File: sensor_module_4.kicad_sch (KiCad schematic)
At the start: 34 parts, among them J1 pH_IN, J17 Atlas Surveyor, J18 EZO Carrier Board, J3 ORP_In, J4 Turbidity TSW-10, U3 ESDA5V3SC5, U4 OPA2397DGKR, U5 OPA2397DGKR

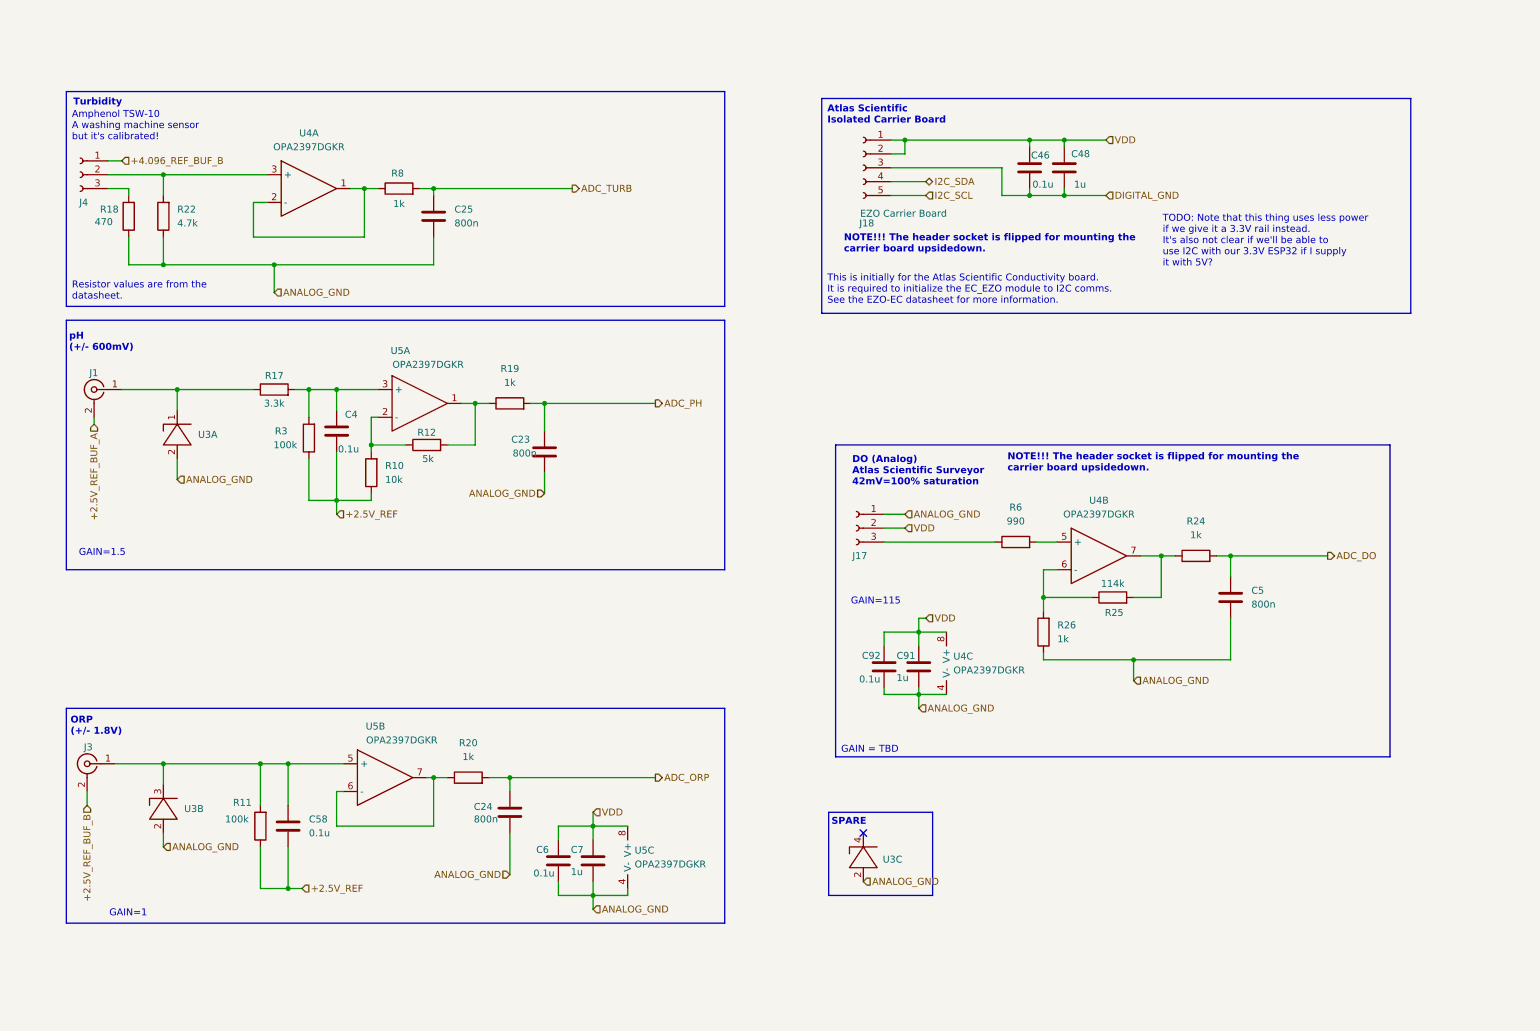
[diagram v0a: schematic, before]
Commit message: Prototype v0.3.1 WIP Just a maintenance checkin. Many changes - Removed the Base Sensor schematic and put all sensors into SensorPrototype - Added a constant current LED driver for camera illumination - Added a 12V buck converter to the input in support of external power - Added a low-side current sense to the input - Added an LDO regulator to cleanup Buck output and to provide battery regulation - Added support for an internal battery + switchover / charge circuit. - Swapped headers for proper board connectors - Added an RS485 transceiver for external + modem communication - Added an additional temperature circuit in support of NTC probes - Incorporated the AS Dissolved Oxygen sensor into the main board - Added DC return path resistors to non-inverting amps - Fixed mixed power domain bug - Moved AS isolated carrier board to 3.3V rail and routed the shutdown pin to en/sh - Moved the DHT20 to the 3.3V rail - In the process of re-routing ADC channels.
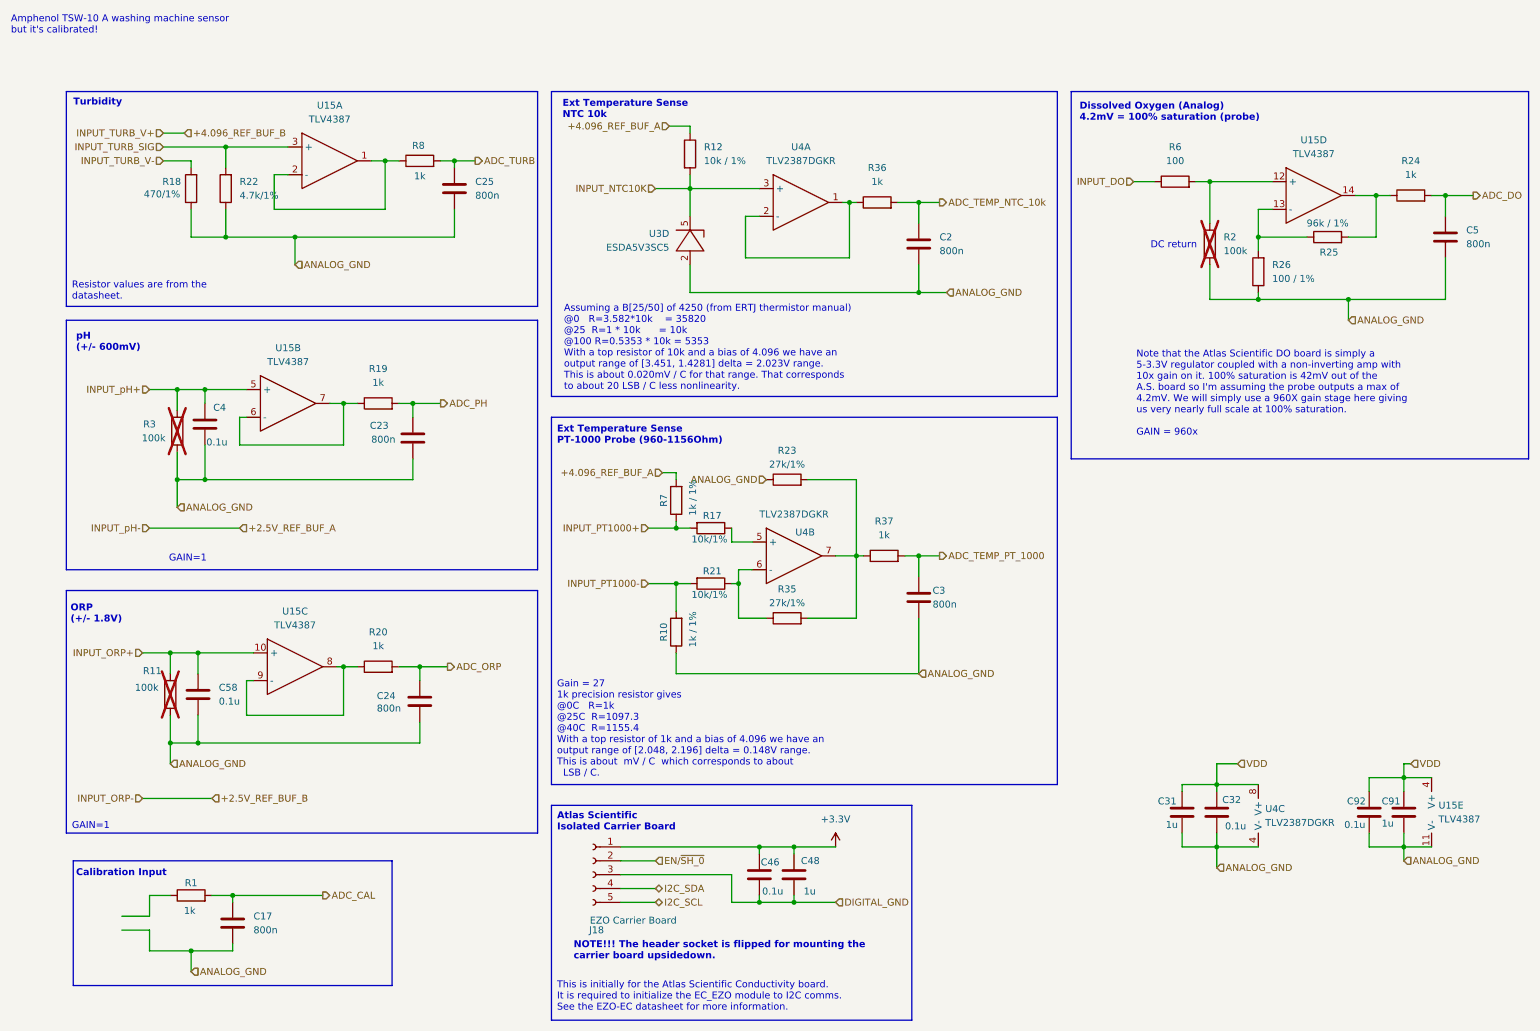
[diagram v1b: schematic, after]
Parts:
- removed C6: 0.1u, Capacitor_SMD:C_1210_3225Metric_Pad1.33x2.70mm_HandSolder, symbol Device:C
- removed C7: 1u, Capacitor_SMD:C_1210_3225Metric_Pad1.33x2.70mm_HandSolder, symbol Device:C
- removed J1: pH_IN, Connector_PinHeader_2.54mm:PinHeader_1x02_P2.54mm_Vertical_SMD_Pin1Left, symbol Connector:Conn_Coaxial
- removed J17: Atlas Surveyor, Connector_PinSocket_2.54mm:PinSocket_1x03_P2.54mm_Vertical, symbol Connector:Conn_01x03_Socket
- removed J3: ORP_In, Connector_PinHeader_2.54mm:PinHeader_1x02_P2.54mm_Vertical_SMD_Pin1Left, symbol Connector:Conn_Coaxial
- removed J4: Turbidity TSW-10, Connector_PinHeader_2.54mm:PinHeader_1x03_P2.54mm_Vertical_SMD_Pin1Left, symbol Connector:Conn_01x03_Socket
- removed U3: ESDA5V3SC5, Package_TO_SOT_SMD:SOT-23-5, symbol AndrewAdditions:sda5v3sc6_split
- removed U4, U5: OPA2397DGKR, Package_SO:SOIC-8_3.9x4.9mm_P1.27mm, symbol Op-Amp-Extended:OPA2397DR
- added C17, C2, C3: 800n, Capacitor_SMD:C_0805_2012Metric_Pad1.18x1.45mm_HandSolder, symbol Device:C
- added C31: 1u, Capacitor_SMD:C_0805_2012Metric_Pad1.18x1.45mm_HandSolder, symbol Device:C
- added C32: 0.1u, Capacitor_SMD:C_0805_2012Metric_Pad1.18x1.45mm_HandSolder, symbol Device:C
- added R1, R36, R37: 1k, Resistor_SMD:R_0805_2012Metric_Pad1.20x1.40mm_HandSolder, symbol Device:R
- added R2: 100k, Resistor_SMD:R_0805_2012Metric_Pad1.20x1.40mm_HandSolder, symbol Device:R
- added R21: 10k/1%, Resistor_SMD:R_0805_2012Metric_Pad1.20x1.40mm_HandSolder, symbol Device:R
- added R23, R35: 27k/1%, Resistor_SMD:R_0805_2012Metric_Pad1.20x1.40mm_HandSolder, symbol Device:R
- added R7: 1k / 1%, Resistor_SMD:R_0805_2012Metric_Pad1.20x1.40mm_HandSolder, symbol Device:R
- added U15: TLV4387, Package_SO:TSSOP-14_4.4x5mm_P0.65mm, symbol Op-Amp-Extended:TLV4387PWR
- added U3: ESDA5V3SC5, Package_TO_SOT_SMD:SOT-23-5, symbol AndrewAdditions:sda5v3sc6_split
- added U4: TLV2387DGKR, Package_SO:VSSOP-8_3x3mm_P0.65mm, symbol Op-Amp-Extended:TLV2387DGKR
- C23, C24, C25, C4, C46, C48, C5, C58, C91, C92: footprint Capacitor_SMD:C_1210_3225Metric_Pad1.33x2.70mm_HandSolder -> Capacitor_SMD:C_0805_2012Metric_Pad1.18x1.45mm_HandSolder
- J18: footprint Connector_PinSocket_2.54mm:PinSocket_1x05_P2.54mm_Vertical -> Connector_PinSocket_2.54mm:PinSocket_1x05_P2.54mm_Vertical_SMD_Pin1Left
- R10: value 10k -> 1k / 1%; footprint Resistor_SMD:R_1210_3225Metric_Pad1.30x2.65mm_HandSolder -> Resistor_SMD:R_0805_2012Metric_Pad1.20x1.40mm_HandSolder
- R11, R3: footprint Resistor_SMD:R_1210_3225Metric_Pad1.30x2.65mm_HandSolder -> Resistor_SMD:R_0805_2012Metric_Pad1.20x1.40mm_HandSolder; now not fitted
- R12: value 5k -> 10k / 1%; footprint Resistor_SMD:R_1210_3225Metric_Pad1.30x2.65mm_HandSolder -> (none)
- R17: value 3.3k -> 10k/1%; footprint Resistor_SMD:R_1210_3225Metric_Pad1.30x2.65mm_HandSolder -> Resistor_SMD:R_0805_2012Metric_Pad1.20x1.40mm_HandSolder
- R18: value 470 -> 470/1%; footprint Resistor_SMD:R_1210_3225Metric_Pad1.30x2.65mm_HandSolder -> Resistor_SMD:R_0805_2012Metric_Pad1.20x1.40mm_HandSolder
- R19, R20, R24, R8: footprint Resistor_SMD:R_1210_3225Metric_Pad1.30x2.65mm_HandSolder -> Resistor_SMD:R_0805_2012Metric_Pad1.20x1.40mm_HandSolder
- R22: value 4.7k -> 4.7k/1%; footprint Resistor_SMD:R_1210_3225Metric_Pad1.30x2.65mm_HandSolder -> Resistor_SMD:R_0805_2012Metric_Pad1.20x1.40mm_HandSolder
- R25: value 114k -> 96k / 1%; footprint Resistor_SMD:R_1210_3225Metric_Pad1.30x2.65mm_HandSolder -> Resistor_SMD:R_0805_2012Metric_Pad1.20x1.40mm_HandSolder
- R26: value 1k -> 100 / 1%; footprint Resistor_SMD:R_1210_3225Metric_Pad1.30x2.65mm_HandSolder -> Resistor_SMD:R_0805_2012Metric_Pad1.20x1.40mm_HandSolder
- R6: value 990 -> 100; footprint Resistor_SMD:R_1210_3225Metric_Pad1.30x2.65mm_HandSolder -> Resistor_SMD:R_0805_2012Metric_Pad1.20x1.40mm_HandSolder
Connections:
- net +2.5V_REF is gone; now on net ANALOG_GND: C4.2, C58.2, R10.1, R11.1, R3.1
- net ANALOG_GND: now also C17.2, C2.2, C3.2, C31.2, C32.2, R2.1, R23.1, U15.11 (V-), U3.2, U4.4 (V-)
- net VDD: now also C31.1, C32.1, U15.4 (V+), U4.8 (V+); no longer C46.1, C48.1, J18.1 (Pin_1), J18.2 (Pin_2)
- net at R17.1: now also U4.5 (+)
- net INPUT_TURB_V-: now reaches R18.2
- net at R25.1, R26.2: now also U15.13 (-)
- net at R19.1: now also U15.6 (-), U15.7; no longer R12.2
- net at R8.1: now also U15.1, U15.2 (-)
- net INPUT_ORP+: now reaches C58.1, R11.2
- net INPUT_ORP+: now also U15.10 (+)
- net at R20.1: now also U15.8, U15.9 (-)
- net INPUT_pH+: now reaches C4.1, R3.2
- net INPUT_pH+: now also U15.5 (+); no longer R17.2
- net INPUT_TURB_SIG: now reaches R22.2
- net INPUT_TURB_SIG: now also U15.3 (+)
- net +4.096_REF_BUF_A: now reaches R12.1
- net +4.096_REF_BUF_A: now also R7.2; no longer R10.2
- net INPUT_DO: now reaches R6.1
- net at R6.2: now also R2.2, U15.12 (+)
- net at R24.1, R25.2: now also U15.14
- new net: R21.1, R35.1, U4.6 (-)
- new net: R36.1, U4.1, U4.2 (-)
- new net: R23.2, R35.2, R37.1, U4.7
- new net +3.3V: C46.1, C48.1, J18.1 (Pin_1)
- new net ADC_CAL: C17.1, R1.2
- new net ADC_TEMP_NTC_10k: C2.1, R36.2
- new net ADC_TEMP_PT_1000: C3.1, R37.2
- new net EN/~{SH_0}: J18.2 (Pin_2)
- new net INPUT_NTC10K: R12.2, U3.5, U4.3 (+)
- new net INPUT_PT1000+: R17.2, R7.1
- new net INPUT_PT1000-: R10.2, R21.2
- no-connect marks 1 -> 0
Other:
- note added: "Assuming a B[25/50] of 4250 (from ERTJ thermistor manual) @0 R=3.582*10k = 35820 @25 R=1 * 10k = 10k @100 R=0.5353 * 10k = 5353 With a top resistor of 10k and a bias of 4.096 we have an output range of [3.451, 1.4281] delta = 2.023V range. This is about 0.020mV / C for that range. That corresponds to about 20 LSB / C less nonlinearity."
- note added: "Calibration Input"
- note added: "DC return"
- note added: "Dissolved Oxygen (Analog) 4.2mV = 100% saturation (probe)"
- note added: "Ext Temperature Sense NTC 10k"
- note added: "Ext Temperature Sense PT-1000 Probe (960-1156Ohm)"
- note added: "Gain = 27 1k precision resistor gives @0C R=1k @25C R=1097.3 @40C R=1155.4 With a top resistor of 1k and a bias of 4.096 we have an output range of [2.048, 2.196] delta = 0.148V range. This is about mV / C which corresponds to about LSB / C."
- note added: "Note that the Atlas Scientific DO board is simply a 5-3.3V regulator coupled with a non-inverting amp with 10x gain on it. 100% saturation is 42mV out of the A.S. board so I'm assuming the probe outputs a max of 4.2mV. We will simply use a 960X gain stage here giving us very nearly full scale at 100% saturation. GAIN = 960x"
- note removed: "DO (Analog) Atlas Scientific Surveyor 42mV=100% saturation"
- note removed: "GAIN = TBD"
- note removed: "GAIN=1.5"
- note removed: "GAIN=115"
- note removed: "SPARE"
- note removed: "TODO: Note that this thing uses less power if we give it a 3.3V rail instead. It's also not clear if we'll be able to use I2C with our 3.3V ESP32 if I supply it with 5V?"
- moved on the sheet: C23, C24, C25, C4, C46, C48, C5, C58, C91, C92, J18, R18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

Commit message: Board V0.0.3 Everything is routed and connected ERC and DRC run without serious error. (There are DRC violations due to a VSSP-83x3mm package but I'm not sure why)
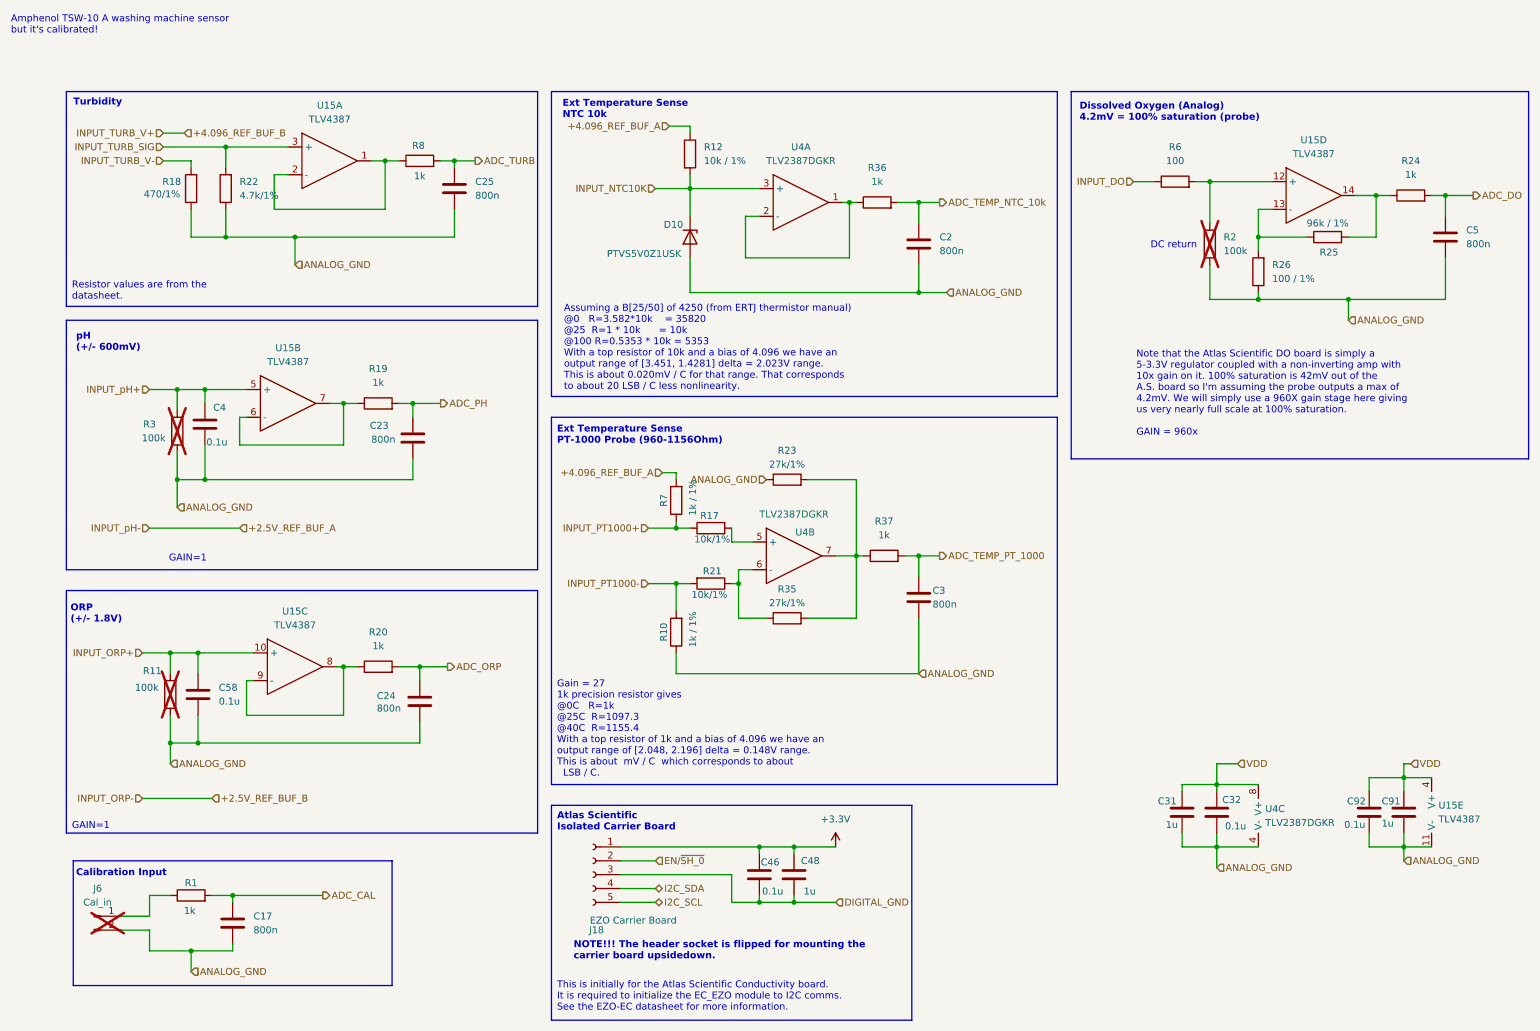
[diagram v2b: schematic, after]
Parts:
- removed U3: ESDA5V3SC5, Package_TO_SOT_SMD:SOT-23-5, symbol AndrewAdditions:sda5v3sc6_split
- added D10: PTVS5V0Z1USK, Diode_SMD:Nexperia_DSN1608-2_1.6x0.8mm, symbol Diode:PTVS5V0Z1USK
- added J6: Cal_in, Connector_PinHeader_2.54mm:PinHeader_1x02_P2.54mm_Vertical_SMD_Pin1Left, symbol Connector:Conn_01x02_Pin
- R12: footprint (none) -> Resistor_SMD:R_0805_2012Metric_Pad1.20x1.40mm_HandSolder
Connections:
- net ANALOG_GND: now also D10.2 (A), J6.2 (Pin_2)
- net INPUT_NTC10K: now also D10.1 (K)
- net INPUT_PT1000+: now also R17.1; no longer R17.2
- net at U4.5 (+): now also R17.2; no longer R17.1
- net at R1.1: now also J6.1 (Pin_1)
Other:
- moved on the sheet: R17
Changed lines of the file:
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@@
 	(wire
 		(pts
-			(xy 128.27 52.07) (xy 128.27 46.99)
+			(xy 128.27 45.72) (xy 128.27 52.07)
 		)
 		(stroke
@@
 	(symbol
 		(lib_id "Device:R")
-		(at 132.08 95.25 270)
+		(at 132.08 95.25 90)
+		(mirror x)
 		(unit 1)
 		(exclude_from_sim no)
@@
 		(dnp no)
 		(property "Reference" "R17"
-			(at 132.334 92.964 90)
+			(at 131.826 92.964 90)
 			(effects
 				(font
@@
 		)
 		(property "Value" "10k/1%"
-			(at 131.826 97.282 90)
+			(at 132.334 97.282 90)
 			(effects
 				(font
@@
 	)
 	(symbol
-		(lib_id "AndrewAdditions:sda5v3sc6_split")
-		(at 128.27 41.91 0)
-		(mirror y)
-		(unit 4)
-		(exclude_from_sim no)
-		(in_bom yes)
-		(on_board yes)
-		(dnp no)
-		(property "Reference" "U3"
-			(at 124.46 41.2749 0)
-			(effects
-				(font
-					(size 1.27 1.27)
-				)
-				(justify left)
-			)
-		)
-		(property "Value" "ESDA5V3SC5"
-			(at 124.46 43.8149 0)
-			(effects
-				(font
-					(size 1.27 1.27)
-				)
-				(justify left)
-			)
-		)
-		(property "Footprint" "Package_TO_SOT_SMD:SOT-23-5"
-			(at 128.27 41.91 0)
-			(effects
-				(font
-					(size 1.27 1.27)
-				)
-				(hide yes)
-			)
-		)
-		(property "Datasheet" "https://www.st.com/resource/en/datasheet/esda5v3sc6.pdf"
-			(at 128.27 41.91 0)
-			(effects
-				(font
-					(size 1.27 1.27)
-				)
-				(hide yes)
-			)
-		)
-		(property "Description" "Quad TVS Diode Array, 5.3V Standoff, 4 Channels, 400W, ±30kV, SOT-23-5 Keywords: usb esd protection suppression transient"
-			(at 128.27 41.91 0)
-			(effects
-				(font
-					(size 1.27 1.27)
-				)
-				(hide yes)
-			)
-		)
-		(property "Resistance" ""
-			(at 128.27 41.91 0)
-			(effects
-				(font
-					(size 1.27 1.27)
-				)
-				(hide yes)
-			)
-		)
-		(pin "5"
-		)
-		(pin "3"
-		)
-		(pin "2"
-		)
-		(pin "1"
-		)
-		(pin "4"
-		)
-		(instances
-			(project "digital_waters"
-				(path "/37fdfe07-1a70-41c8-8af2-e03e19737580/569ba513-db4e-4a75-8161-f5cfa6b9cf84"
-					(reference "U3")
-					(unit 4)
-				)
-			)
-		)
-	)
-	(symbol
 		(lib_id "Device:C")
 		(at 170.18 107.95 0)
@@
 	)
 	(symbol
+		(lib_id "Connector:Conn_01x02_Pin")
+		(at 19.05 166.37 0)
+		(unit 1)
+		(exclude_from_sim no)
+		(in_bom yes)
+		(on_board yes)
+		(dnp yes)
+		(fields_autoplaced yes)
+		(property "Reference" "J6"
+			(at 19.685 161.29 0)
+			(effects
+				(font
+					(size 1.27 1.27)
+				)
+			)
+		)
+		(property "Value" "Cal_in"
+			(at 19.685 163.83 0)
+			(effects
+				(font
+					(size 1.27 1.27)
+				)
+			)
+		)
+		(property "Footprint" "Connector_PinHeader_2.54mm:PinHeader_1x02_P2.54mm_Vertical_SMD_Pin1Left"
+			(at 19.05 166.37 0)
+			(effects
+				(font
+					(size 1.27 1.27)
+				)
+				(hide yes)
+			)
+		)
+		(property "Datasheet" "~"
+			(at 19.05 166.37 0)
+			(effects
+				(font
+					(size 1.27 1.27)
+				)
+				(hide yes)
+			)
+		)
+		(property "Description" "Generic connector, single row, 01x02, script generated"
+			(at 19.05 166.37 0)
+			(effects
+				(font
+					(size 1.27 1.27)
+				)
+				(hide yes)
+			)
+		)
+		(pin "2"
+		)
+		(pin "1"
+		)
+		(instances
+			(project ""
+				(path "/37fdfe07-1a70-41c8-8af2-e03e19737580/569ba513-db4e-4a75-8161-f5cfa6b9cf84"
+					(reference "J6")
+					(unit 1)
+				)
+			)
+		)
+	)
+	(symbol
 		(lib_id "Device:C")
 		(at 266.7 41.91 0)
@@
 			)
 		)
-		(property "Footprint" ""
+		(property "Footprint" "Resistor_SMD:R_0805_2012Metric_Pad1.20x1.40mm_HandSolder"
 			(at 126.492 26.67 90)
 			(effects
@@
 					(unit 1)
 				)
+			)
+		)
+	)
+	(symbol
+		(lib_id "Diode:PTVS5V0Z1USK")
+		(at 128.27 41.91 270)
+		(unit 1)
+		(exclude_from_sim no)
+		(in_bom yes)
+		(on_board yes)
+		(dnp no)
+		(property "Reference" "D10"
+			(at 123.444 39.624 90)
+			(effects
+				(font
+					(size 1.27 1.27)
+				)
+				(justify left)
+			)
+		)
+		(property "Value" "PTVS5V0Z1USK"
+			(at 113.03 44.958 90)
+			(effects
+				(font
+					(size 1.27 1.27)
+				)
+				(justify left)
+			)
+		)
+		(property "Footprint" "Diode_SMD:Nexperia_DSN1608-2_1.6x0.8mm"
+			(at 123.825 41.91 0)
+			(effects
+				(font
+					(size 1.27 1.27)
+				)
+				(hide yes)
+			)
+		)
+		(property "Datasheet" "https://assets.nexperia.com/documents/data-sheet/PTVS5V0Z1USK.pdf"
+			(at 128.27 41.91 0)
+			(effects
+				(font
+					(size 1.27 1.27)
+				)
+				(hide yes)
+			)
+		)
+		(property "Description" "5V, 1200W TVS unidirectional diode, DSN1608-2"
+			(at 128.27 41.91 0)
+			(effects
+				(font
+					(size 1.27 1.27)
+				)
+				(hide yes)
+			)
+		)
+		(pin "1"
+		)
+		(pin "2"
+		)
+		(instances
+			(project ""
+				(path "/37fdfe07-1a70-41c8-8af2-e03e19737580/569ba513-db4e-4a75-8161-f5cfa6b9cf84"
+					(reference "D10")
+					(unit 1)
+				)
